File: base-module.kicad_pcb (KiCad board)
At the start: 4 copper layers, 111 parts, among them J200 09031967921, Q700 S9013, U300 TPS563201DDCR, U301 TPS563201DDCR, U402 TS3USB30ERSWR, U403 IP4234CZ6,115, U404 IP4234CZ6,115, U406 CH334R, U407 STM32F750V8Tx, U501 TJA1044GTK_3Z, U602 TJA1044GTK_3Z, U700 STM32F103CBTx, X402 X322512MSB4SI, X700 X50328MSB2GI, Y403 12Mhz

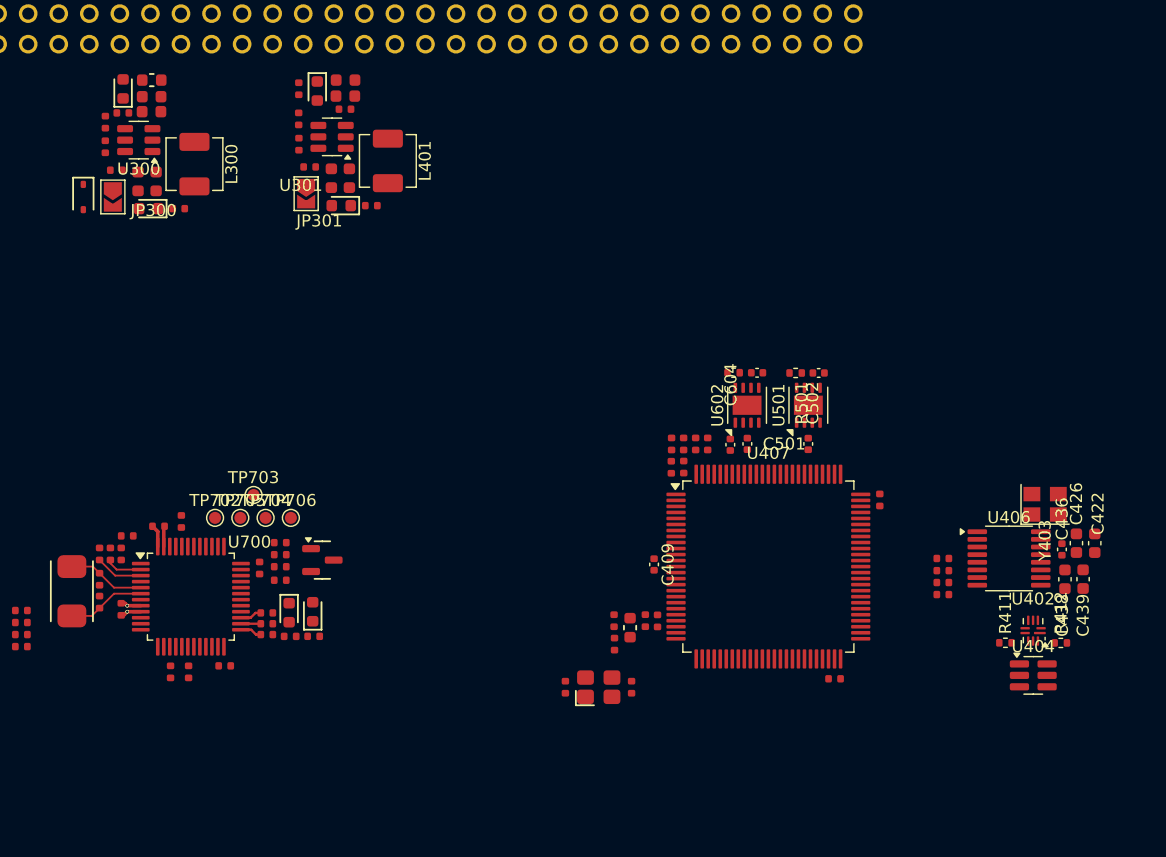
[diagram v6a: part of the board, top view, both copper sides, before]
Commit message: [2] Add footprints
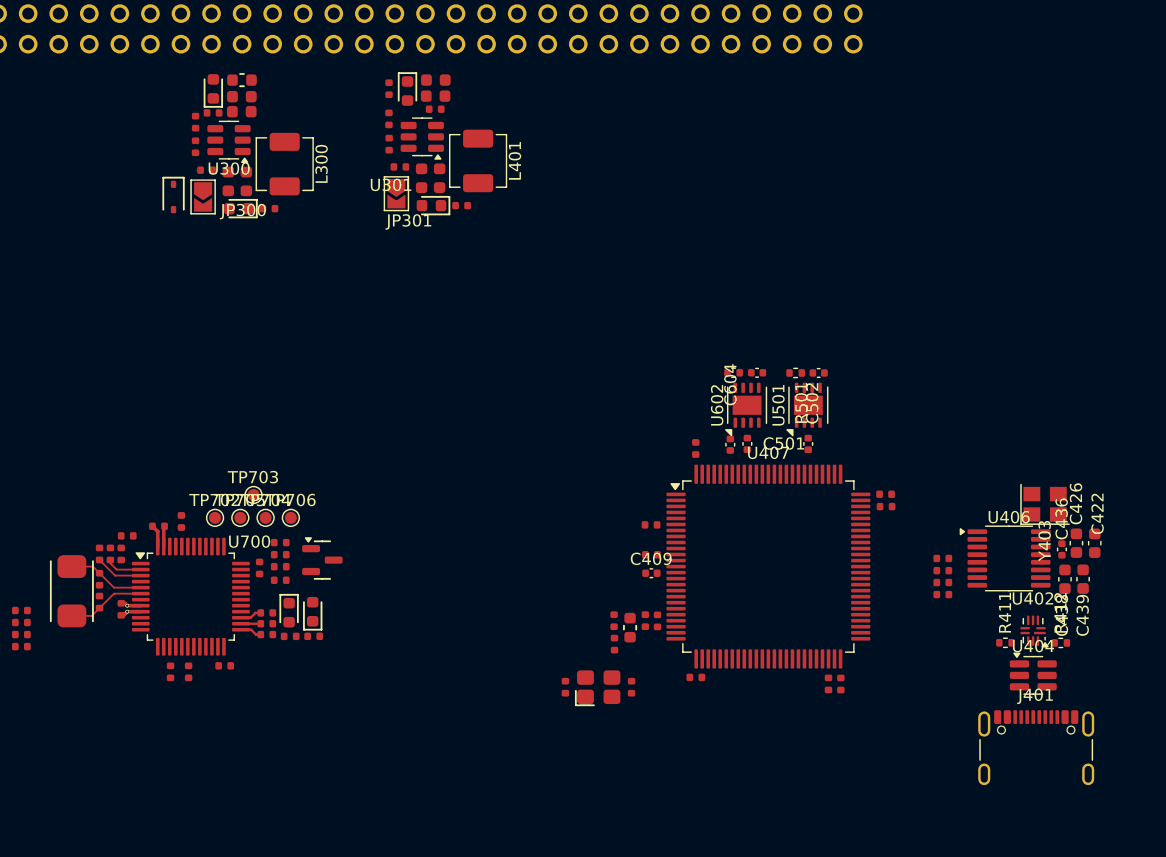
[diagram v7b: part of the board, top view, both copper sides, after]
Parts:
- added J401: USB_C_Receptacle_USB2.0_16P, Connector_USB:USB_C_Receptacle_GCT_USB4105-xx-A_16P_TopMnt_Horizontal, F.Cu at (129.8, 148.7)
- moved C401 24.4 mm to (113.5, 142.3), turned to -90 degrees
- moved C406 17.6 mm to (101.5, 141.7), turned to 180 degrees
- moved C402 17.3 mm to (117.2, 126.5), turned to 0 degrees
- moved C403 9.92 mm to (97.8, 131.5), turned to 180 degrees
- moved C404 8.21 mm to (97.7, 129.0), turned to 180 degrees
- moved L300 7.50 mm to (67.3, 99.1)
- moved C300 7.50 mm to (60.8, 99.6)
- moved C301 7.50 mm to (62.6, 100.5)
- moved C302 7.50 mm to (64.1, 100.5)
- moved C303 7.50 mm to (63.7, 94.7)
- moved C304 7.50 mm to (63.7, 93.4)
- moved C305 7.50 mm to (76.9, 99.3)
- moved C306 7.50 mm to (80.2, 100.2)
- moved C307 7.50 mm to (78.7, 100.2)
- moved C308 7.50 mm to (79.8, 93.4)
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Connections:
- net /MCU/PA11 renamed /MCU/USBIN1.D-
- net /MCU/PA12 renamed /MCU/USBIN1.D+
- net /MCU/PA13 renamed /MCU/SWD.SWDIO
- net /MCU/PA14 renamed /MCU/SWD.SWCLK
- U407 pad 96: /MCU/I2C1.SCL -> /MCU/I2C1.SDA

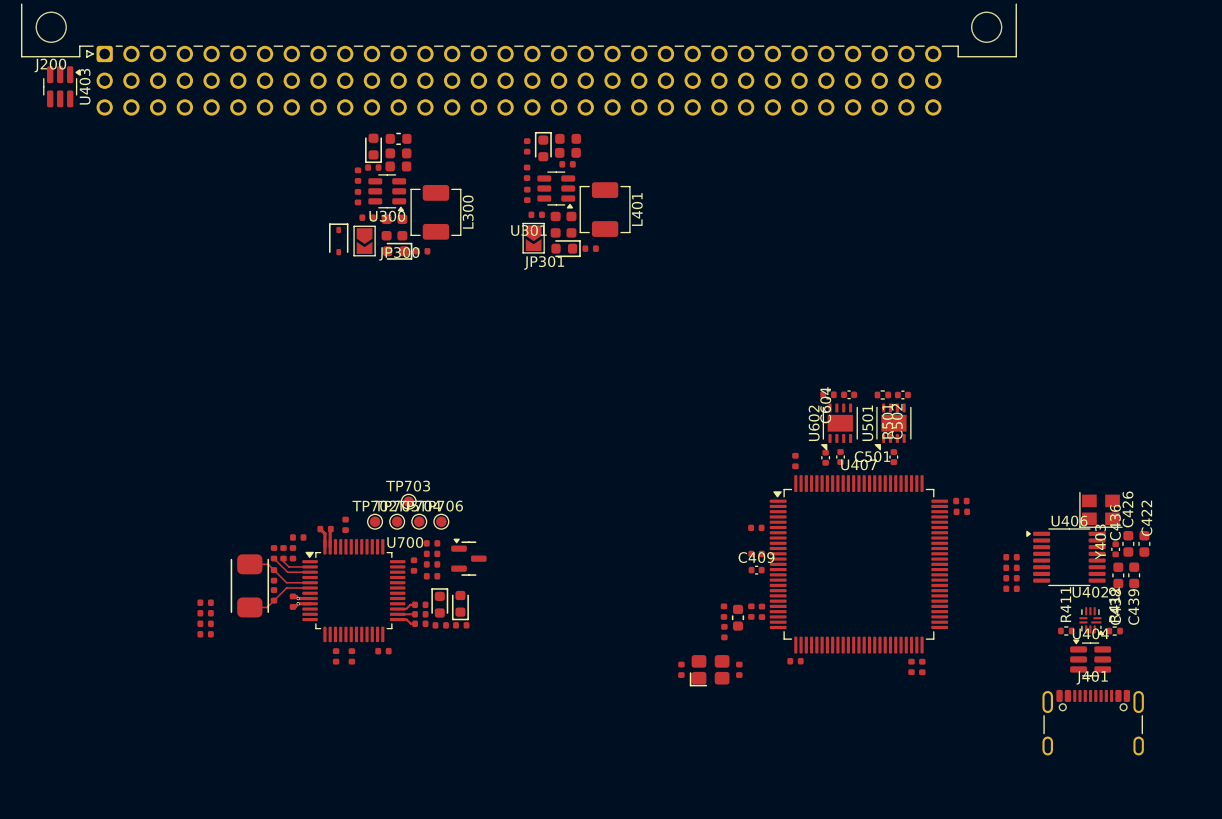
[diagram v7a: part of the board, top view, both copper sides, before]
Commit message: [2] Fix component placements
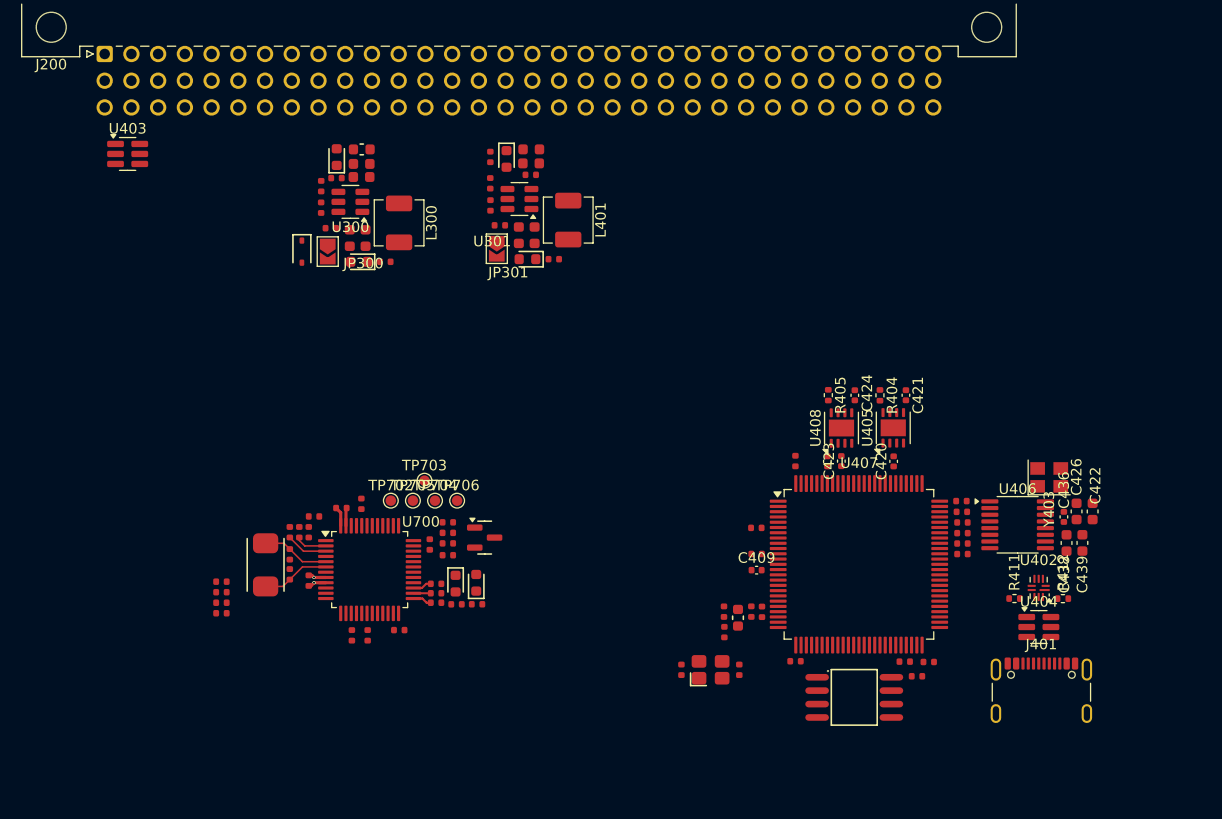
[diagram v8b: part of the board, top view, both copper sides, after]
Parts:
- removed C501, C502, C603, C604: 100nF, Capacitor_SMD:C_0402_1005Metric
- removed R501, R602: 10k, Resistor_SMD:R_0402_1005Metric
- removed U501, U602: TJA1044GTK_3Z, Package_SON:HVSON-8-1EP_3x3mm_P0.65mm_EP1.6x2.4mm
- added C420: 100nF, Capacitor_SMD:C_0402_1005Metric, F.Cu at (110.8, 122.7)
- added C421: 100nF, Capacitor_SMD:C_0402_1005Metric, F.Cu at (112.0, 116.4)
- added C423: 100nF, Capacitor_SMD:C_0402_1005Metric, F.Cu at (105.8, 122.7)
- added C424: 100nF, Capacitor_SMD:C_0402_1005Metric, F.Cu at (107.1, 116.4)
- added C425: 100nF, PCM_JLCPCB:C_0402, F.Cu at (113.0, 143.1)
- added R404: 10k, Resistor_SMD:R_0402_1005Metric, F.Cu at (109.5, 116.4)
- added R405: 10k, Resistor_SMD:R_0402_1005Metric, F.Cu at (104.6, 116.4)
- added U401: W25Q128, PCM_JLCPCB:SOIC-8_L5.3-W5.3-P1.27-LS8.0-BL, F.Cu at (107.1, 145.1)
- added U405: TJA1044GTK_3Z, Package_SON:HVSON-8-1EP_3x3mm_P0.65mm_EP1.6x2.4mm, F.Cu at (110.8, 119.5)
- added U408: TJA1044GTK_3Z, Package_SON:HVSON-8-1EP_3x3mm_P0.65mm_EP1.6x2.4mm, F.Cu at (105.8, 119.5)
- moved U403 9.04 mm to (38.0, 93.5), turned to 0 degrees
- moved J401 5.81 mm to (124.8, 145.6)
- moved R412 5.81 mm to (126.9, 135.8)
- moved C436 5.81 mm to (127.0, 128.0)
- moved R411 5.81 mm to (122.3, 135.8)
- moved Y403 5.81 mm to (125.6, 124.2)
- moved C422 5.81 mm to (129.7, 127.5)
- moved C426 5.81 mm to (128.2, 127.5)
- moved C438 5.81 mm to (127.2, 130.5)
- moved U402 5.81 mm to (124.6, 134.7)
- moved U404 5.81 mm to (124.6, 138.5)
- moved U406 5.81 mm to (122.6, 128.7)
- moved C439 5.81 mm to (128.7, 130.5)
- moved R443 5.71 mm to (117.3, 128.5)
- moved R444 5.71 mm to (117.3, 129.5)
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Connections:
- net /MCU/SWD.SWCLK renamed /MCU/PA14
- net /MCU/SWD.SWDIO renamed /MCU/PA13
- net /ST-LINK/SWCLK renamed /ST-LINK/SWD.SWCLK
- net /ST-LINK/SWDIO renamed /ST-LINK/SWD.SWDIO
- R443 pad 1: /USB-hub/USBOUT2.D- -> /MCU/USB_MCU.-
- R444 pad 1: /USB-hub/USBOUT2.D+ -> /MCU/USB_MCU.+
- R708 pad 1: /MCU/NRST -> /ST-LINK/~{RST}
- U407 pad 1: /MCU/PE2 -> /MCU/QSPI1.IO2
- U407 pad 14: /MCU/NRST -> /MCU/~{RST}
- U407 pad 36: /MCU/PB2 -> /MCU/QSPI1.SCLK
- U407 pad 58: /MCU/PD11 -> /MCU/QSPI1.IO0
- U407 pad 59: /MCU/PD12 -> /MCU/QSPI1.IO1
- U407 pad 60: /MCU/PD13 -> /MCU/QSPI1.IO3
- U407 pad 70: /MCU/USBIN1.D- -> /MCU/USB_MCU.-
- U407 pad 71: /MCU/USBIN1.D+ -> /MCU/USB_MCU.+
- U407 pad 81: /MCU/CAN1.RX -> /CAN transceiver 1/CAN.RX
- U407 pad 82: /MCU/CAN1.TX -> /CAN transceiver 1/CAN.TX
- U407 pad 91: /MCU/CAN2.RX -> /CAN transceiver 2/CAN.RX
- U407 pad 92: /MCU/CAN2.TX -> /CAN transceiver 2/CAN.TX
- U407 pad 96: /MCU/I2C1.SDA -> /MCU/I2C1.SCL
